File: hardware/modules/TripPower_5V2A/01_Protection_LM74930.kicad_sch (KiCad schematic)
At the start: 40 parts, among them J301 INPUT: VIN/RUN/GND, J302 OUT: PROT_UNFUSED/5V/GND, Q301 SQM10250E_GE3 250V CANDIDATE, Q302 BUK7Y4R8-60EX 60V CANDIDATE, U301 LM74930QRGERQ1

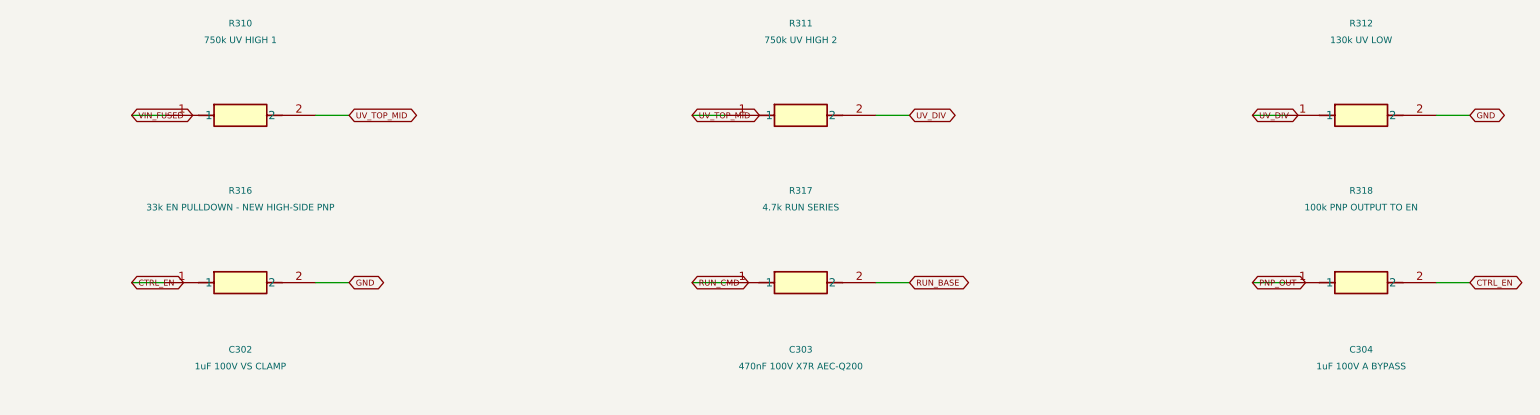
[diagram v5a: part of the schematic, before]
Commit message: refactor(TripPower): set PNP-source EN 68k/22k divider for 9V HIGH margin, lower hot OFF leakage voltage and reduced 56V power
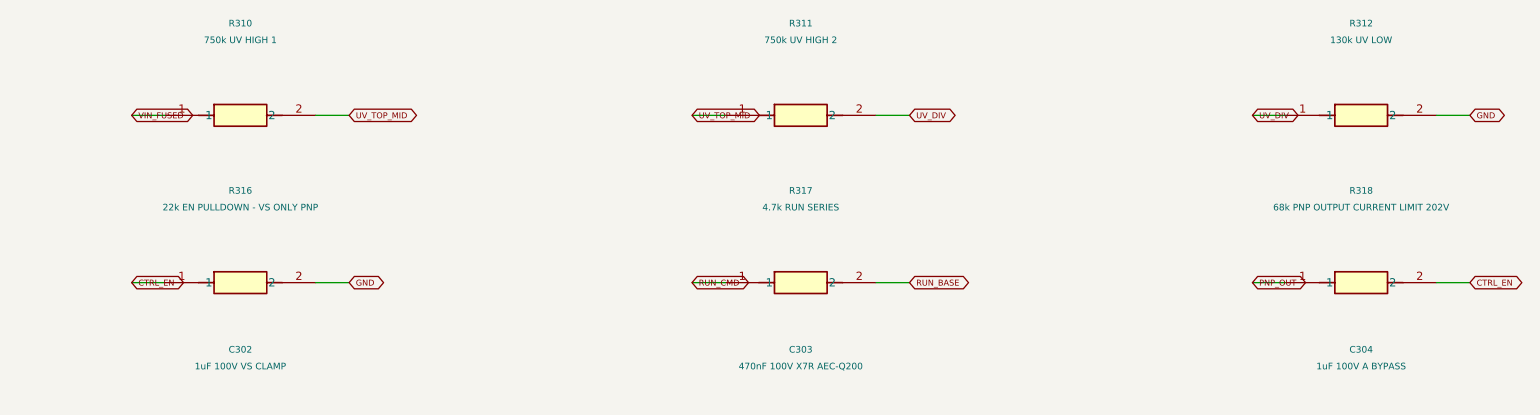
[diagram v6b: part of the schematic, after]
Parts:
- R316: value 33k EN PULLDOWN - NEW HIGH-SIDE PNP -> 22k EN PULLDOWN - VS ONLY PNP
- R318: value 100k PNP OUTPUT TO EN -> 68k PNP OUTPUT CURRENT LIMIT 202V
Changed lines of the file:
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@@
 (symbol (lib_id "Tripmaster_Sym:R") (at 149.86 275.59 0) (unit 1) (in_bom yes) (on_board yes) (dnp no) (property "Reference" "R314" (at 149.86 261.62 0) (effects (font (size 1 1)))) (property "Value" "3.3k 2512 PULSE CANDIDATE" (at 149.86 264.16 0) (effects (font (size 1 1)))) (property "Footprint" "Resistor_SMD:R_2512_6332Metric" (at 149.86 275.59 0) (effects (font (size 1.0 1.0)) (hide yes))) (property "MPN" "CRCW25123K30FKEGHP" (at 0 0 0) (effects (font (size 1 1)) (hide yes))) (pin "1") (pin "2") (instances (project "TripPower_5V2A" (path "/f1512578-cc72-4c26-bf70-dbbd00000001/f1512578-cc72-4c26-bf70-dbbd00000002" (reference "R314") (unit 1)))))
 (symbol (lib_id "Tripmaster_Sym:R") (at 234.95 275.59 0) (unit 1) (in_bom yes) (on_board yes) (dnp no) (property "Reference" "R315" (at 234.95 261.62 0) (effects (font (size 1 1)))) (property "Value" "3.3k 2512 PULSE CANDIDATE" (at 234.95 264.16 0) (effects (font (size 1 1)))) (property "Footprint" "Resistor_SMD:R_2512_6332Metric" (at 234.95 275.59 0) (effects (font (size 1.0 1.0)) (hide yes))) (property "MPN" "CRCW25123K30FKEGHP" (at 0 0 0) (effects (font (size 1 1)) (hide yes))) (pin "1") (pin "2") (instances (project "TripPower_5V2A" (path "/f1512578-cc72-4c26-bf70-dbbd00000001/f1512578-cc72-4c26-bf70-dbbd00000002" (reference "R315") (unit 1)))))
-(symbol (lib_id "Tripmaster_Sym:R") (at 320.04 275.59 0) (unit 1) (in_bom yes) (on_board yes) (dnp no) (property "Reference" "R316" (at 320.04 261.62 0) (effects (font (size 1 1)))) (property "Value" "33k EN PULLDOWN - NEW HIGH-SIDE PNP" (at 320.04 264.16 0) (effects (font (size 1 1)))) (property "Footprint" "Tripmaster:R_1206_3216" (at 320.04 275.59 0) (effects (font (size 1.0 1.0)) (hide yes))) (pin "1") (pin "2") (instances (project "TripPower_5V2A" (path "/f1512578-cc72-4c26-bf70-dbbd00000001/f1512578-cc72-4c26-bf70-dbbd00000002" (reference "R316") (unit 1)))))
+(symbol (lib_id "Tripmaster_Sym:R") (at 320.04 275.59 0) (unit 1) (in_bom yes) (on_board yes) (dnp no) (property "Reference" "R316" (at 320.04 261.62 0) (effects (font (size 1 1)))) (property "Value" "22k EN PULLDOWN - VS ONLY PNP" (at 320.04 264.16 0) (effects (font (size 1 1)))) (property "Footprint" "Tripmaster:R_1206_3216" (at 320.04 275.59 0) (effects (font (size 1.0 1.0)) (hide yes))) (pin "1") (pin "2") (instances (project "TripPower_5V2A" (path "/f1512578-cc72-4c26-bf70-dbbd00000001/f1512578-cc72-4c26-bf70-dbbd00000002" (reference "R316") (unit 1)))))
 (symbol (lib_id "Tripmaster_Sym:R") (at 405.13 275.59 0) (unit 1) (in_bom yes) (on_board yes) (dnp no) (property "Reference" "R317" (at 405.13 261.62 0) (effects (font (size 1 1)))) (property "Value" "4.7k RUN SERIES" (at 405.13 264.16 0) (effects (font (size 1 1)))) (property "Footprint" "Tripmaster:R_1206_3216" (at 405.13 275.59 0) (effects (font (size 1.0 1.0)) (hide yes))) (pin "1") (pin "2") (instances (project "TripPower_5V2A" (path "/f1512578-cc72-4c26-bf70-dbbd00000001/f1512578-cc72-4c26-bf70-dbbd00000002" (reference "R317") (unit 1)))))
-(symbol (lib_id "Tripmaster_Sym:R") (at 490.22 275.59 0) (unit 1) (in_bom yes) (on_board yes) (dnp no) (property "Reference" "R318" (at 490.22 261.62 0) (effects (font (size 1 1)))) (property "Value" "100k PNP OUTPUT TO EN" (at 490.22 264.16 0) (effects (font (size 1 1)))) (property "Footprint" "Tripmaster:R_1206_3216" (at 490.22 275.59 0) (effects (font (size 1.0 1.0)) (hide yes))) (pin "1") (pin "2") (instances (project "TripPower_5V2A" (path "/f1512578-cc72-4c26-bf70-dbbd00000001/f1512578-cc72-4c26-bf70-dbbd00000002" (reference "R318") (unit 1)))))
+(symbol (lib_id "Tripmaster_Sym:R") (at 490.22 275.59 0) (unit 1) (in_bom yes) (on_board yes) (dnp no) (property "Reference" "R318" (at 490.22 261.62 0) (effects (font (size 1 1)))) (property "Value" "68k PNP OUTPUT CURRENT LIMIT 202V" (at 490.22 264.16 0) (effects (font (size 1 1)))) (property "Footprint" "Tripmaster:R_1206_3216" (at 490.22 275.59 0) (effects (font (size 1.0 1.0)) (hide yes))) (pin "1") (pin "2") (instances (project "TripPower_5V2A" (path "/f1512578-cc72-4c26-bf70-dbbd00000001/f1512578-cc72-4c26-bf70-dbbd00000002" (reference "R318") (unit 1)))))
 (symbol (lib_id "Tripmaster_Sym:R") (at 64.77 299.72 0) (unit 1) (in_bom yes) (on_board yes) (dnp no) (property "Reference" "R319" (at 64.77 285.75 0) (effects (font (size 1 1)))) (property "Value" "0R POPULATE FOR ALWAYS_ON" (at 64.77 288.29 0) (effects (font (size 1 1)))) (property "Footprint" "Tripmaster:R_1206_3216" (at 64.77 299.72 0) (effects (font (size 1.0 1.0)) (hide yes))) (pin "1") (pin "2") (instances (project "TripPower_5V2A" (path "/f1512578-cc72-4c26-bf70-dbbd00000001/f1512578-cc72-4c26-bf70-dbbd00000002" (reference "R319") (unit 1)))))
 (symbol (lib_id "Tripmaster_Sym:R") (at 149.86 299.72 0) (unit 1) (in_bom yes) (on_board yes) (dnp no) (property "Reference" "R320" (at 149.86 285.75 0) (effects (font (size 1 1)))) (property "Value" "100R dVdt-C SERIES (TI)" (at 149.86 288.29 0) (effects (font (size 1 1)))) (property "Footprint" "Tripmaster:R_1206_3216" (at 149.86 299.72 0) (effects (font (size 1.0 1.0)) (hide yes))) (pin "1") (pin "2") (instances (project "TripPower_5V2A" (path "/f1512578-cc72-4c26-bf70-dbbd00000001/f1512578-cc72-4c26-bf70-dbbd00000002" (reference "R320") (unit 1)))))

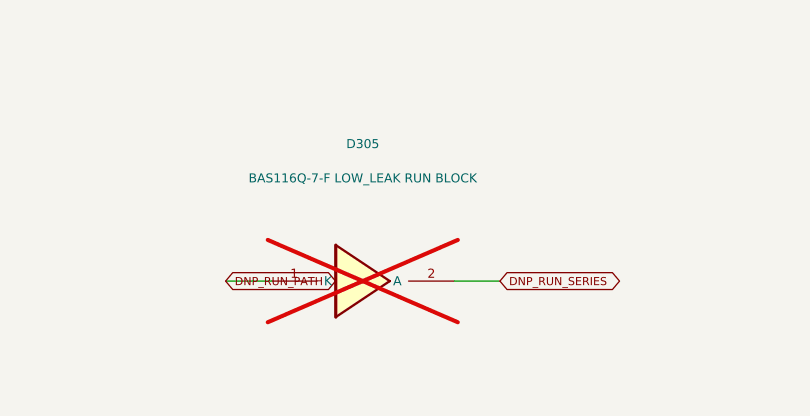
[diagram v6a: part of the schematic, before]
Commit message: fix(TripPower): isolate USB RUN backfeed with automotive BAS116Q K3/A1/NC2 SOT23 diode in READY/RUN series sink
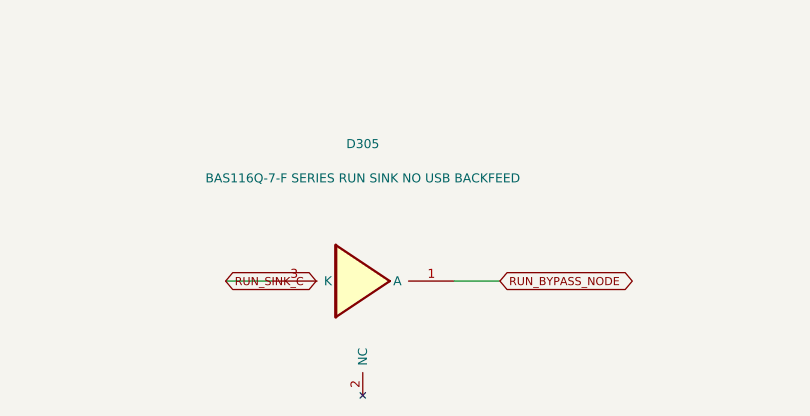
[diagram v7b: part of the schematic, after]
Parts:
- D305: value BAS116Q-7-F LOW_LEAK RUN BLOCK -> BAS116Q-7-F SERIES RUN SINK NO USB BACKFEED; footprint Diode_SMD:D_SOD-323 -> Package_TO_SOT_SMD:SOT-23; symbol TripTracer_V1:PWR_DIODE -> TripPower_Sym:BAS116Q_A1_K3_NC2; now fitted
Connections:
- net DNP_RUN_PATH is gone; now on net RUN_BYPASS_NODE: D305.1 (A)
- net DNP_RUN_SERIES: no longer names the net of D305.2 (NC)
- new net RUN_SINK_C: D305.3 (K)
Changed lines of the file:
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@@
 (global_label "FAULT_OC_N" (shape bidirectional) (at 48.26 400.05 0) (effects (font (size 0.9 0.9)) (justify left)))
 (global_label "5V_OUT" (shape bidirectional) (at 81.28 400.05 0) (effects (font (size 0.9 0.9)) (justify left)))
-(symbol (lib_id "TripTracer_V1:PWR_DIODE") (at 151.13 400.05 0) (unit 1) (in_bom yes) (on_board yes) (dnp yes)
+(symbol (lib_id "TripPower_Sym:BAS116Q_A1_K3_NC2") (at 151.13 400.05 0) (unit 1) (in_bom yes) (on_board yes) (dnp no)
 (property "Reference" "D305" (at 151.13 384.81 0) (effects (font (size 1 1))))
-(property "Value" "BAS116Q-7-F LOW_LEAK RUN BLOCK" (at 151.13 388.62 0) (effects (font (size 1 1))))
-(property "Footprint" "Diode_SMD:D_SOD-323" (at 151.13 400.05 0) (effects (font (size 1 1)) (hide yes)))
-(pin "1") (pin "2")
+(property "Value" "BAS116Q-7-F SERIES RUN SINK NO USB BACKFEED" (at 151.13 388.62 0) (effects (font (size 1 1))))
+(property "Footprint" "Package_TO_SOT_SMD:SOT-23" (at 151.13 400.05 0) (effects (font (size 1 1)) (hide yes)))
+(pin "1") (pin "3") (pin "2")
 (instances (project "TripPower_5V2A" (path "/f1512578-cc72-4c26-bf70-dbbd00000001/f1512578-cc72-4c26-bf70-dbbd00000002" (reference "D305") (unit 1)))))
 (wire (pts (xy 140.97 400.05) (xy 135.89 400.05)) (stroke (width 0) (type default)))
-(global_label "DNP_RUN_PATH" (shape bidirectional) (at 135.89 400.05 0) (effects (font (size 0.9 0.9)) (justify left)))
+(global_label "RUN_SINK_C" (shape bidirectional) (at 135.89 400.05 0) (effects (font (size 0.9 0.9)) (justify left)))
 (wire (pts (xy 161.29 400.05) (xy 166.37 400.05)) (stroke (width 0) (type default)))
-(global_label "DNP_RUN_SERIES" (shape bidirectional) (at 166.37 400.05 0) (effects (font (size 0.9 0.9)) (justify left)))
+(global_label "RUN_BYPASS_NODE" (shape bidirectional) (at 166.37 400.05 0) (effects (font (size 0.9 0.9)) (justify left)))
 (symbol (lib_id "Tripmaster_Sym:C") (at 149.86 350.52 0) (unit 1) (in_bom yes) (on_board yes) (dnp no) (property "Reference" "C307" (at 149.86 336.55 0) (effects (font (size 1 1)))) (property "Value" "10nF 250V dVdt WIP" (at 149.86 339.09 0) (effects (font (size 1 1)))) (property "Footprint" "Tripmaster:C_1206_3216" (at 149.86 350.52 0) (effects (font (size 1.0 1.0)) (hide yes))) (property "MPN" "C1206C103JARECAUTO" (at 0 0 0) (effects (font (size 1 1)) (hide yes))) (property "Datasheet" "https://www.digikey.de/en/products/detail/kemet/C1206C103JARECAUTO/16680107" (at 0 0 0) (effects (font (size 1 1)) (hide yes))) (pin "1") (pin "2") (instances (project "TripPower_5V2A" (path "/f1512578-cc72-4c26-bf70-dbbd00000001/f1512578-cc72-4c26-bf70-dbbd00000002" (reference "C307") (unit 1)))))
 (wire (pts (xy 138.43 350.52) (xy 133.35 350.52)) (stroke (width 0) (type default)))

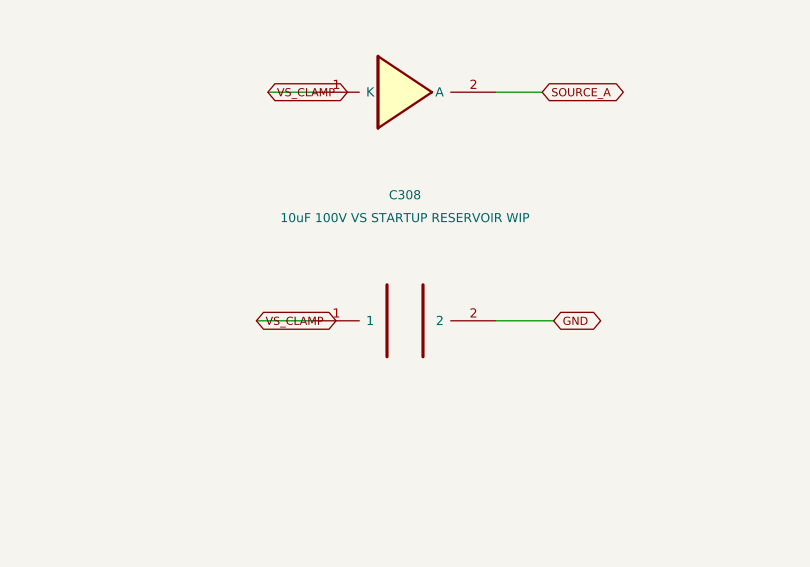
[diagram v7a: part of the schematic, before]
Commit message: feat(TripPower REV4): use automotive 100V 10uF Flexiterm MLCC for VS hold-up, with corrected nonpolar nets
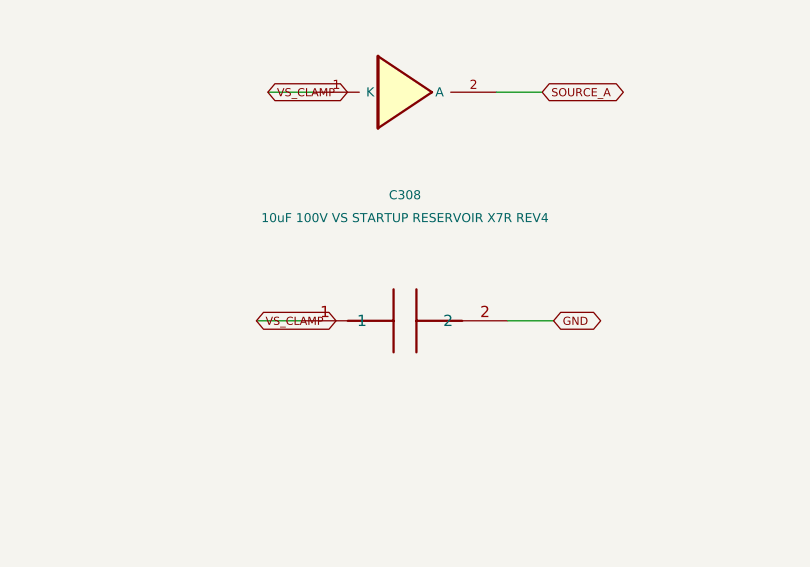
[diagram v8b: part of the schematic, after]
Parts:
- C308: value 10uF 100V VS STARTUP RESERVOIR WIP -> 10uF 100V VS STARTUP RESERVOIR X7R REV4; footprint Capacitor_SMD:CP_Elec_8x10.5 -> Capacitor_SMD:C_2220_5750Metric; symbol TripTracer_V1:PWR_CPOL -> Tripmaster_Sym:C; MPN EEE-TG2A100P -> KAF55CR72A106KV; Supplier_URL https://www.digikey.de/en/products/detail/panasonic-industr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 -> https://www.mouser.de/de/ProductDetail/KYOCERA-AVX/KAF55CR7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
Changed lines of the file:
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@@
 (wire (pts (xy 161.29 350.52) (xy 166.37 350.52)) (stroke (width 0) (type default)))
 (global_label "GND" (shape bidirectional) (at 166.37 350.52 0) (effects (font (size 0.9 0.9)) (justify left)))
-(symbol (lib_id "TripTracer_V1:PWR_CPOL") (at 320.04 350.52 0) (unit 1) (in_bom yes) (on_board yes) (dnp no) (property "Reference" "C308" (at 320.04 336.55 0) (effects (font (size 1 1)))) (property "Value" "10uF 100V VS STARTUP RESERVOIR WIP" (at 320.04 339.09 0) (effects (font (size 1 1)))) (property "Footprint" "Capacitor_SMD:CP_Elec_8x10.5" (at 320.04 350.52 0) (effects (font (size 1.0 1.0)) (hide yes))) (property "MPN" "EEE-TG2A100P" (at 0 0 0) (effects (font (size 1 1)) (hide yes))) (property "Supplier_URL" "https://www.digikey.de/en/products/detail/panasonic-industry/EEE-TG2A100P/817792" (at 0 0 0) (effects (font (size 1 1)) (hide yes))) (pin "1") (pin "2") (instances (project "TripPower_5V2A" (path "/f1512578-cc72-4c26-bf70-dbbd00000001/f1512578-cc72-4c26-bf70-dbbd00000002" (reference "C308") (unit 1)))))
-(wire (pts (xy 309.88 350.52) (xy 303.53 350.52)) (stroke (width 0) (type default)))
+(symbol (lib_id "Tripmaster_Sym:C") (at 320.04 350.52 0) (unit 1) (in_bom yes) (on_board yes) (dnp no) (property "Reference" "C308" (at 320.04 336.55 0) (effects (font (size 1 1)))) (property "Value" "10uF 100V VS STARTUP RESERVOIR X7R REV4" (at 320.04 339.09 0) (effects (font (size 1 1)))) (property "Footprint" "Capacitor_SMD:C_2220_5750Metric" (at 320.04 350.52 0) (effects (font (size 1.0 1.0)) (hide yes))) (property "MPN" "KAF55CR72A106KV" (at 0 0 0) (effects (font (size 1 1)) (hide yes))) (property "Supplier_URL" "https://www.mouser.de/de/ProductDetail/KYOCERA-AVX/KAF55CR72A106KV" (at 0 0 0) (effects (font (size 1 1)) (hide yes))) (pin "1") (pin "2") (instances (project "TripPower_5V2A" (path "/f1512578-cc72-4c26-bf70-dbbd00000001/f1512578-cc72-4c26-bf70-dbbd00000002" (reference "C308") (unit 1)))))
+(wire (pts (xy 308.61 350.52) (xy 303.53 350.52)) (stroke (width 0) (type default)))
 (global_label "VS_CLAMP" (shape bidirectional) (at 303.53 350.52 0) (effects (font (size 0.9 0.9)) (justify left)))
-(wire (pts (xy 330.2 350.52) (xy 336.55 350.52)) (stroke (width 0) (type default)))
+(wire (pts (xy 331.47 350.52) (xy 336.55 350.52)) (stroke (width 0) (type default)))
 (global_label "GND" (shape bidirectional) (at 336.55 350.52 0) (effects (font (size 0.9 0.9)) (justify left)))
 (symbol (lib_id "Tripmaster_Sym:C") (at 405.13 350.52 0) (unit 1) (in_bom yes) (on_board yes) (dnp yes) (property "Reference" "C309" (at 405.13 336.55 0) (effects (font (size 1 1)))) (property "Value" "10uF 50V EN DELAY WIP" (at 405.13 339.09 0) (effects (font (size 1 1)))) (property "Footprint" "Capacitor_SMD:C_1210_3225Metric" (at 405.13 350.52 0) (effects (font (size 1.0 1.0)) (hide yes))) (property "MPN" "12105C106K4T2A" (at 0 0 0) (effects (font (size 1 1)) (hide yes))) (property "Supplier_URL" "https://www.mouser.de/de/ProductDetail/KEMET/12105C106K4T2A" (at 0 0 0) (effects (font (size 1 1)) (hide yes))) (property "Status" "DNP; supervisor U302 controls Q303 series enable, no RC delay" (at 0 0 0) (effects (font (size 1 1)) (hide yes))) (pin "1") (pin "2") (instances (project "TripPower_5V2A" (path "/f1512578-cc72-4c26-bf70-dbbd00000001/f1512578-cc72-4c26-bf70-dbbd00000002" (reference "C309") (unit 1)))))
